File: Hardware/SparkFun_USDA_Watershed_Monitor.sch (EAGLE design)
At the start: 116 parts, among them J10 QWIIC_RIGHT_ANGLE, J3 QWIIC_RIGHT_ANGLE, J4 U.FL, J5 RJ45, J7 RJ45, J9 RJ45, Q1 20V/4.2A/52mΩ/1.4W, Q2 20V/0.2A/8MHz/1.2Ω/1Vth, Q3 20V/0.2A/8MHz/1.2Ω/1Vth, Q4 20V/0.2A/8MHz/1.2Ω/1Vth, Q5 20V/4.2A/52mΩ/1.4W, Q7 20V/4.2A/52mΩ/1.4W, U1 ESP-WROOM-3232D, U10 MMC5983MA_QFN16, U11 RFM9XRFM95, U12 NAU7802SOIC, U2 AP3429A, U3 MCP73831, U5 BME680, U6 9DoF IMU, U7 1.8V/100mA, U8 CH340C, U9 ISM330DHCX

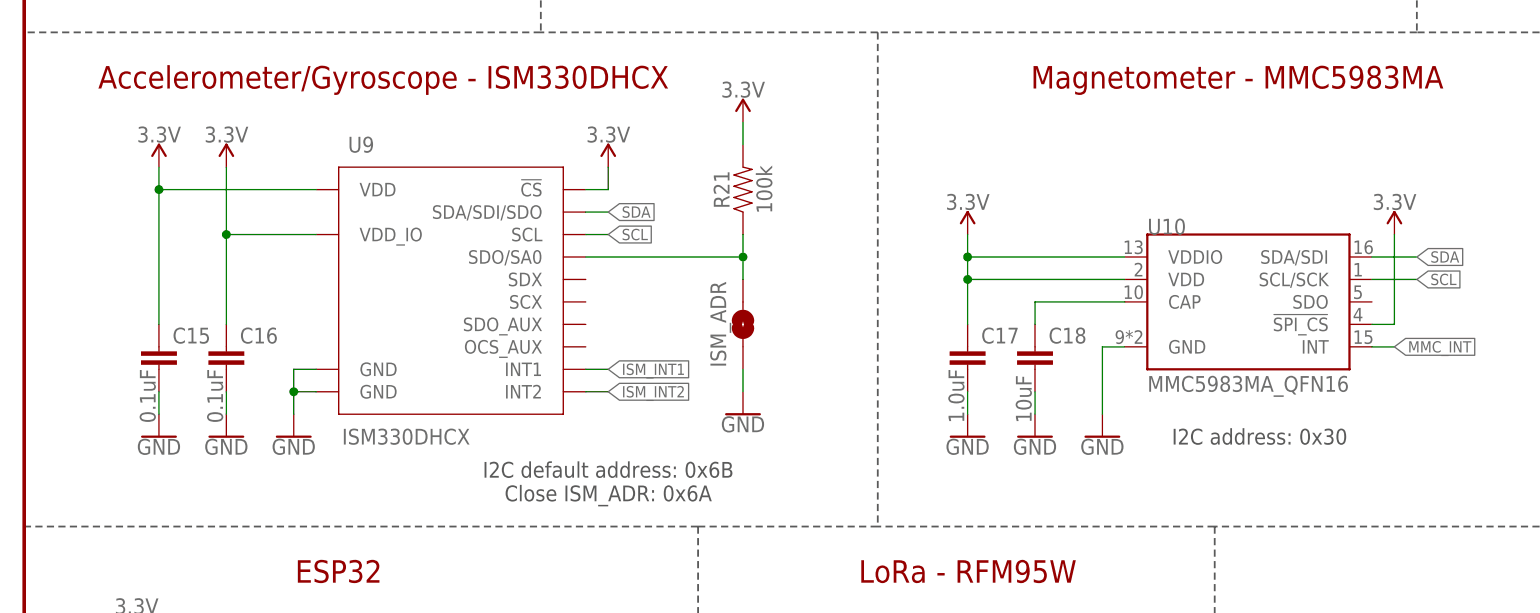
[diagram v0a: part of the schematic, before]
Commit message: Update DNP component values and PROD_ID's
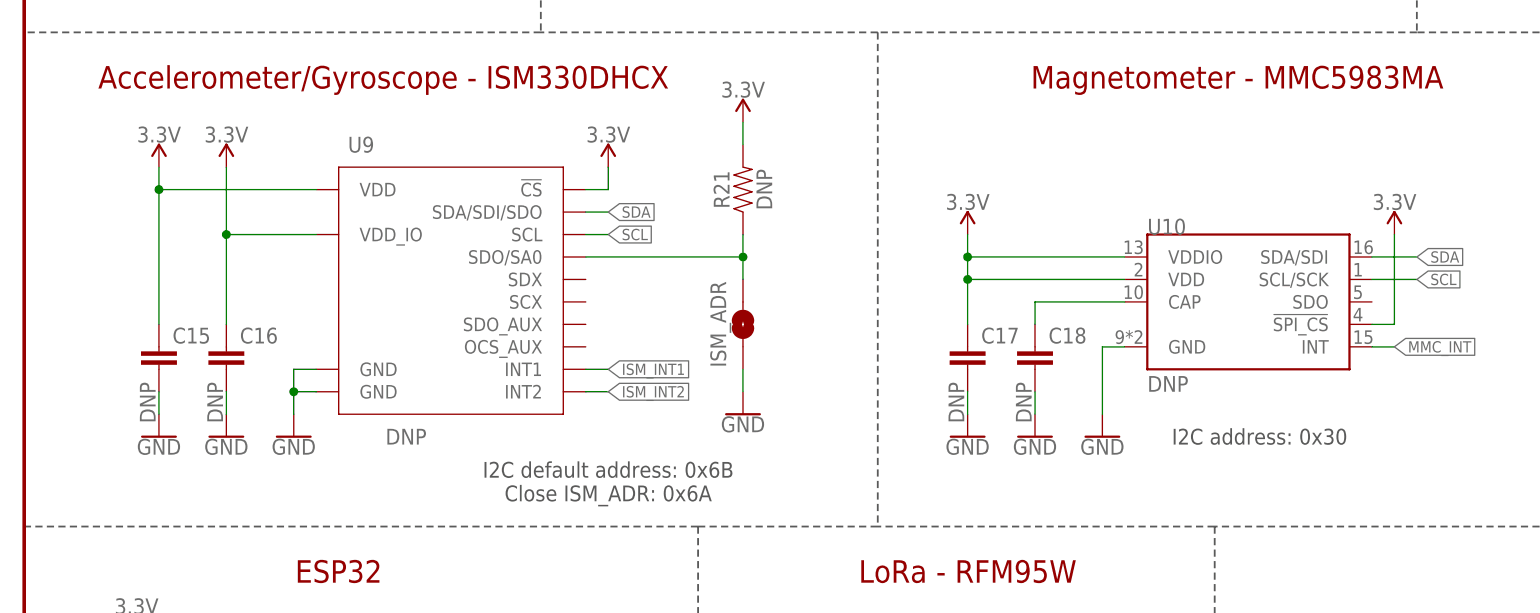
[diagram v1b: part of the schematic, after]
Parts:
- C15, C16: value 0.1uF -> DNP
- C17: value 1.0uF -> DNP
- C18: value 10uF -> DNP
- R21: value 100k -> DNP
- U10: value MMC5983MA_QFN16 -> DNP
- U9: value ISM330DHCX -> DNP
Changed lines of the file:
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@@
 <part name="SUPPLY31" library="SparkFun-PowerSymbols" deviceset="3.3V" device=""/>
 <part name="GND35" library="SparkFun-PowerSymbols" deviceset="GND" device=""/>
-<part name="U9" library="SparkFun-Sensors" deviceset="ISM330DHCX" device=""/>
-<part name="U10" library="SparkFun-Sensors" deviceset="MMC5983MA" device="_QFN16"/>
+<part name="U9" library="SparkFun-Sensors" deviceset="ISM330DHCX" device="" value="DNP">
+<attribute name="PROD_ID" value=""/>
+</part>
+<part name="U10" library="SparkFun-Sensors" deviceset="MMC5983MA" device="_QFN16" value="DNP">
+<attribute name="PROD_ID" value=""/>
+</part>
 <part name="SUPPLY34" library="SparkFun-PowerSymbols" deviceset="3.3V" device=""/>
 <part name="SUPPLY35" library="SparkFun-PowerSymbols" deviceset="3.3V" device=""/>
@@
 <part name="GND37" library="SparkFun-PowerSymbols" deviceset="GND" device=""/>
 <part name="GND38" library="SparkFun-PowerSymbols" deviceset="GND" device=""/>
-<part name="C15" library="SparkFun-Capacitors" deviceset="0.1UF" device="-0603-25V-(+80/-20%)" value="0.1uF"/>
-<part name="C16" library="SparkFun-Capacitors" deviceset="0.1UF" device="-0603-25V-(+80/-20%)" value="0.1uF"/>
+<part name="C15" library="SparkFun-Capacitors" deviceset="0.1UF" device="-0603-25V-(+80/-20%)" value="DNP">
+<attribute name="PROD_ID" value=""/>
+</part>
+<part name="C16" library="SparkFun-Capacitors" deviceset="0.1UF" device="-0603-25V-(+80/-20%)" value="DNP">
+<attribute name="PROD_ID" value=""/>
+</part>
 <part name="GND41" library="SparkFun-PowerSymbols" deviceset="GND" device=""/>
-<part name="C17" library="SparkFun-Capacitors" deviceset="1.0UF" device="-0603-16V-10%" value="1.0uF"/>
-<part name="C18" library="SparkFun-Capacitors" deviceset="10UF" device="-0603-6.3V-20%" value="10uF"/>
+<part name="C17" library="SparkFun-Capacitors" deviceset="1.0UF" device="-0603-16V-10%" value="DNP">
+<attribute name="PROD_ID" value=""/>
+</part>
+<part name="C18" library="SparkFun-Capacitors" deviceset="10UF" device="-0603-6.3V-20%" value="DNP">
+<attribute name="PROD_ID" value=""/>
+</part>
 <part name="GND39" library="SparkFun-PowerSymbols" deviceset="GND" device=""/>
 <part name="GND40" library="SparkFun-PowerSymbols" deviceset="GND" device=""/>
-<part name="R21" library="SparkFun-Resistors" deviceset="100KOHM" device="-0603-1/10W-1%" value="100k"/>
+<part name="R21" library="SparkFun-Resistors" deviceset="100KOHM" device="-0603-1/10W-1%" value="DNP">
+<attribute name="PROD_ID" value=""/>
+</part>
 <part name="SUPPLY37" library="SparkFun-PowerSymbols" deviceset="3.3V" device=""/>
 <part name="GND42" library="SparkFun-PowerSymbols" deviceset="GND" device=""/>

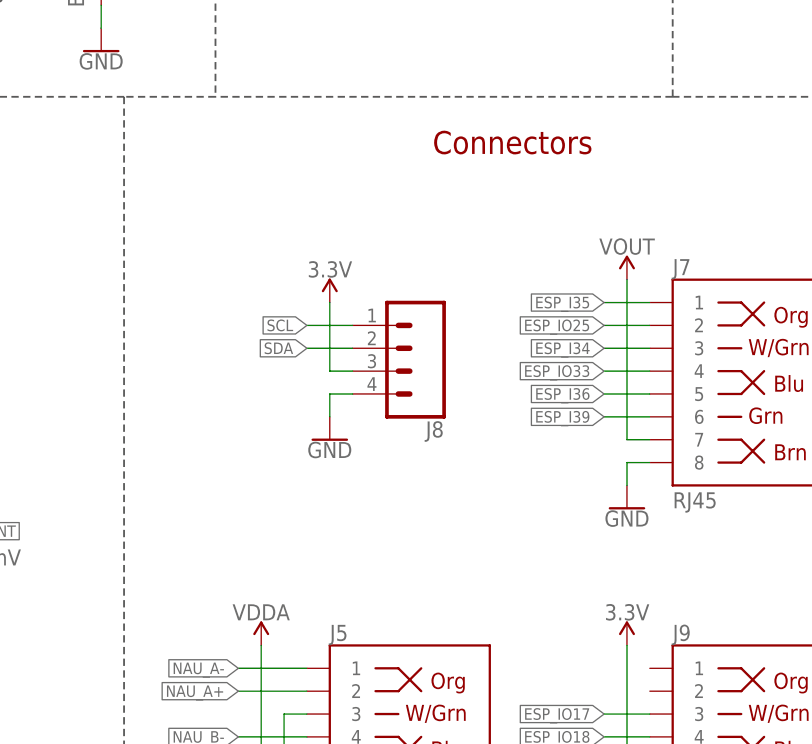
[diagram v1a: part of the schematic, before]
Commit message: Add 3-pin JST connector for GPS
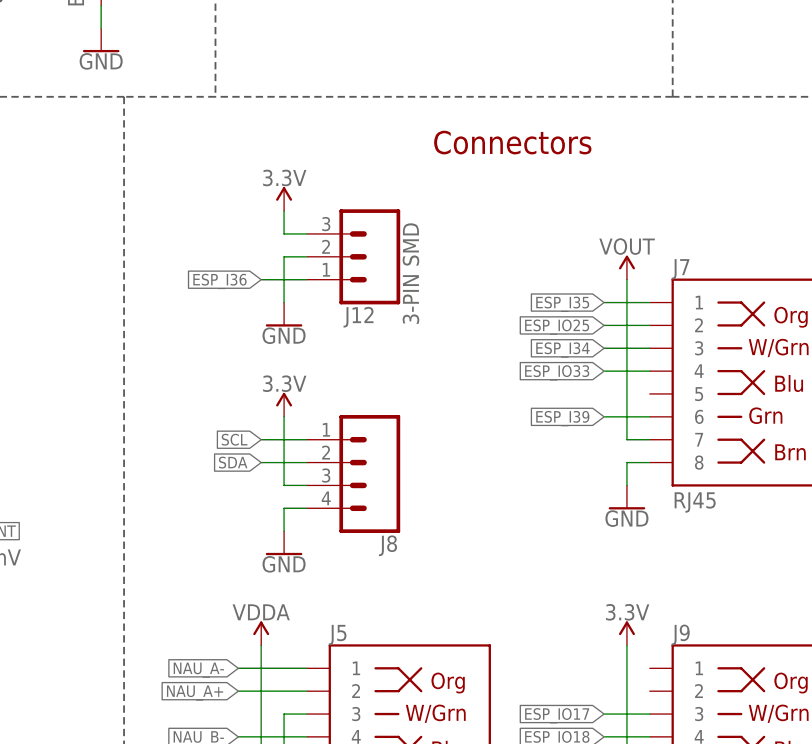
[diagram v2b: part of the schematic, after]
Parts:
- added J12: 3-PIN SMD, SparkFun-Connectors:CONN_03JST-SMD
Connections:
- net 3.3V: now also J12.1
- net ESP_I36: now also J12.3; no longer J7.5
- net GND: now also J12.2
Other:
- moved on the sheet: J8
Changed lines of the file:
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@@
 <part name="SUPPLY10" library="SparkFun-PowerSymbols" deviceset="VOUT" device=""/>
 <part name="R27" library="SparkFun-Resistors" deviceset="100KOHM" device="-0603-1/10W-1%" value="100k"/>
+<part name="J12" library="SparkFun-Connectors" deviceset="CONN_03" device="JST-SMD" value="3-PIN SMD"/>
+<part name="GND61" library="SparkFun-PowerSymbols" deviceset="GND" device=""/>
+<part name="SUPPLY41" library="SparkFun-PowerSymbols" deviceset="3.3V" device=""/>
 </parts>
 <sheets>
@@
 <attribute name="VALUE" x="281.94" y="198.374" size="1.778" layer="96" font="vector" align="bottom-center"/>
 </instance>
-<instance part="J8" gate="J1" x="276.86" y="66.04" smashed="yes" rot="R180">
-<attribute name="VALUE" x="281.94" y="73.406" size="1.778" layer="96" font="vector" rot="R180"/>
-<attribute name="NAME" x="281.94" y="57.912" size="1.778" layer="95" font="vector" rot="R180"/>
+<instance part="J8" gate="J1" x="271.78" y="53.34" smashed="yes" rot="R180">
+<attribute name="VALUE" x="276.86" y="60.706" size="1.778" layer="96" font="vector" rot="R180"/>
+<attribute name="NAME" x="276.86" y="45.212" size="1.778" layer="95" font="vector" rot="R180"/>
 </instance>
 <instance part="J11" gate="G$1" x="48.26" y="259.08" smashed="yes" rot="R180">
@@
 <attribute name="VALUE" x="320.04" y="233.426" size="1.778" layer="96" font="vector" align="top-center"/>
 </instance>
-<instance part="GND59" gate="1" x="269.24" y="55.88" smashed="yes" rot="MR0">
-<attribute name="VALUE" x="269.24" y="55.626" size="1.778" layer="96" font="vector" rot="MR0" align="top-center"/>
-</instance>
-<instance part="SUPPLY6" gate="G$1" x="269.24" y="71.12" smashed="yes" rot="MR0">
-<attribute name="VALUE" x="269.24" y="73.914" size="1.778" layer="96" font="vector" rot="MR0" align="bottom-center"/>
+<instance part="GND59" gate="1" x="264.16" y="43.18" smashed="yes" rot="MR0">
+<attribute name="VALUE" x="264.16" y="42.926" size="1.778" layer="96" font="vector" rot="MR0" align="top-center"/>
+</instance>
+<instance part="SUPPLY6" gate="G$1" x="264.16" y="58.42" smashed="yes" rot="MR0">
+<attribute name="VALUE" x="264.16" y="61.214" size="1.778" layer="96" font="vector" rot="MR0" align="bottom-center"/>
 </instance>
 <instance part="R26" gate="G$1" x="358.14" y="78.74" smashed="yes" rot="R90">
@@
 <attribute name="NAME" x="270.256" y="121.92" size="1.778" layer="95" font="vector" rot="R90" align="bottom-center"/>
 <attribute name="VALUE" x="273.304" y="121.92" size="1.778" layer="96" font="vector" rot="R90" align="top-center"/>
+</instance>
+<instance part="J12" gate="J$1" x="274.32" y="76.2" smashed="yes" rot="R180">
+<attribute name="VALUE" x="279.146" y="68.58" size="1.778" layer="96" font="vector" rot="R90"/>
+<attribute name="NAME" x="274.32" y="70.612" size="1.778" layer="95" font="vector" rot="R180"/>
+</instance>
+<instance part="GND61" gate="1" x="264.16" y="68.58" smashed="yes">
+<attribute name="VALUE" x="264.16" y="68.326" size="1.778" layer="96" font="vector" align="top-center"/>
+</instance>
+<instance part="SUPPLY41" gate="G$1" x="264.16" y="81.28" smashed="yes">
+<attribute name="VALUE" x="264.16" y="84.074" size="1.778" layer="96" font="vector" align="bottom-center"/>
 </instance>
 </instances>
@@
 <segment>
 <pinref part="GND59" gate="1" pin="GND"/>
-<wire x1="271.78" y1="60.96" x2="269.24" y2="60.96" width="0.1524" layer="91"/>
-<wire x1="269.24" y1="60.96" x2="269.24" y2="58.42" width="0.1524" layer="91"/>
+<wire x1="266.7" y1="48.26" x2="264.16" y2="48.26" width="0.1524" layer="91"/>
+<wire x1="264.16" y1="48.26" x2="264.16" y2="45.72" width="0.1524" layer="91"/>
 <pinref part="J8" gate="J1" pin="4"/>
 </segment>
@@
 <wire x1="231.14" y1="175.26" x2="231.14" y2="177.8" width="0.1524" layer="91"/>
 <pinref part="Q4" gate="NMOS" pin="S"/>
+</segment>
+<segment>
+<pinref part="GND61" gate="1" pin="GND"/>
+<pinref part="J12" gate="J$1" pin="2"/>
+<wire x1="264.16" y1="71.12" x2="264.16" y2="76.2" width="0.1524" layer="91"/>
+<wire x1="264.16" y1="76.2" x2="266.7" y2="76.2" width="0.1524" layer="91"/>
 </segment>
 </net>
@@
 <segment>
 <pinref part="SUPPLY6" gate="G$1" pin="3.3V"/>
-<wire x1="271.78" y1="63.5" x2="269.24" y2="63.5" width="0.1524" layer="91"/>
-<wire x1="269.24" y1="63.5" x2="269.24" y2="71.12" width="0.1524" layer="91"/>
+<wire x1="266.7" y1="50.8" x2="264.16" y2="50.8" width="0.1524" layer="91"/>
+<wire x1="264.16" y1="50.8" x2="264.16" y2="58.42" width="0.1524" layer="91"/>
 <pinref part="J8" gate="J1" pin="3"/>
 </segment>
@@
 <junction x="271.78" y="129.54"/>
 </segment>
+<segment>
+<pinref part="J12" gate="J$1" pin="1"/>
+<pinref part="SUPPLY41" gate="G$1" pin="3.3V"/>
+<wire x1="266.7" y1="78.74" x2="264.16" y2="78.74" width="0.1524" layer="91"/>
+<wire x1="264.16" y1="78.74" x2="264.16" y2="81.28" width="0.1524" layer="91"/>
+</segment>
 </net>
 <net name="N$8" class="0">
@@
 </segment>
 <segment>
-<wire x1="271.78" y1="68.58" x2="266.7" y2="68.58" width="0.1524" layer="91"/>
-<label x="266.7" y="68.58" size="1.27" layer="95" font="vector" rot="MR0" xref="yes"/>
+<wire x1="266.7" y1="55.88" x2="261.62" y2="55.88" width="0.1524" layer="91"/>
+<label x="261.62" y="55.88" size="1.27" layer="95" font="vector" rot="MR0" xref="yes"/>
 <pinref part="J8" gate="J1" pin="1"/>
 </segment>
@@
 </segment>
 <segment>
-<label x="266.7" y="66.04" size="1.27" layer="95" font="vector" rot="MR0" xref="yes"/>
-<wire x1="271.78" y1="66.04" x2="266.7" y2="66.04" width="0.1524" layer="91"/>
+<label x="261.62" y="53.34" size="1.27" layer="95" font="vector" rot="MR0" xref="yes"/>
+<wire x1="266.7" y1="53.34" x2="261.62" y2="53.34" width="0.1524" layer="91"/>
 <pinref part="J8" gate="J1" pin="2"/>
 </segment>
@@
 </segment>
 <segment>
-<wire x1="304.8" y1="60.96" x2="299.72" y2="60.96" width="0.1524" layer="91"/>
-<label x="299.72" y="60.96" size="1.27" layer="95" font="vector" rot="R180" xref="yes"/>
-<pinref part="J7" gate="JP1" pin="5"/>
-</segment>
-</net>
+<wire x1="266.7" y1="73.66" x2="261.62" y2="73.66" width="0.1524" layer="91"/>
+<label x="261.62" y="73.66" size="1.27" layer="95" font="vector" rot="R180" xref="yes"/>
+<pinref part="J12" gate="J$1" pin="3"/>
+</segment>
+</net>

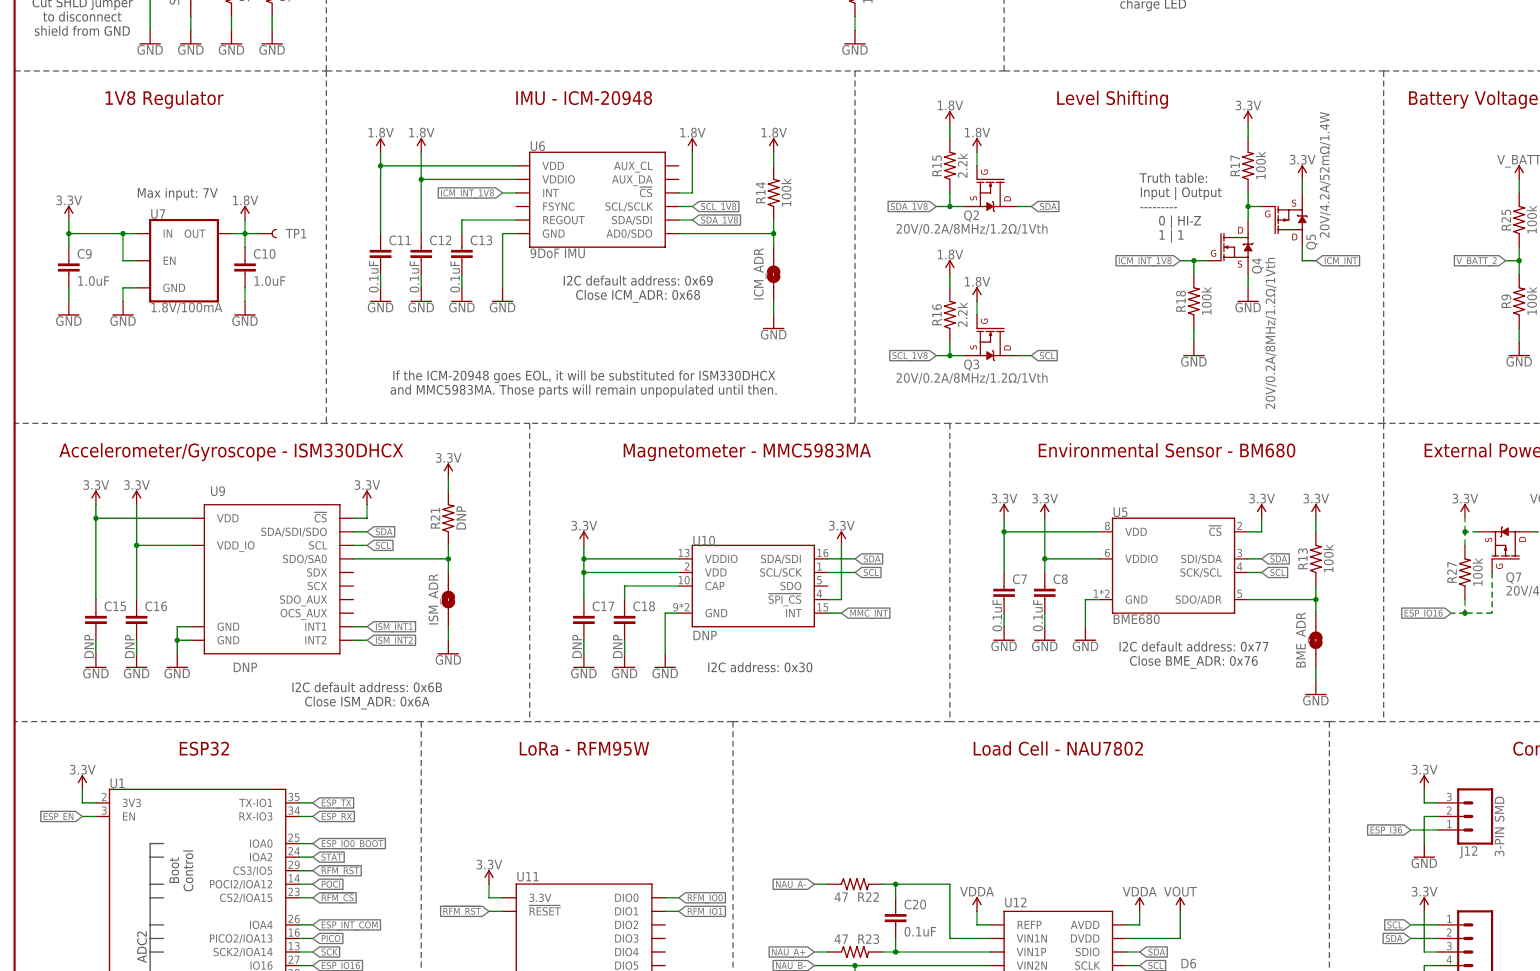
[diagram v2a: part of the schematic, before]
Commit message: Connect all onboard sensors and LoRa to VOUT
Helps achieve lower power
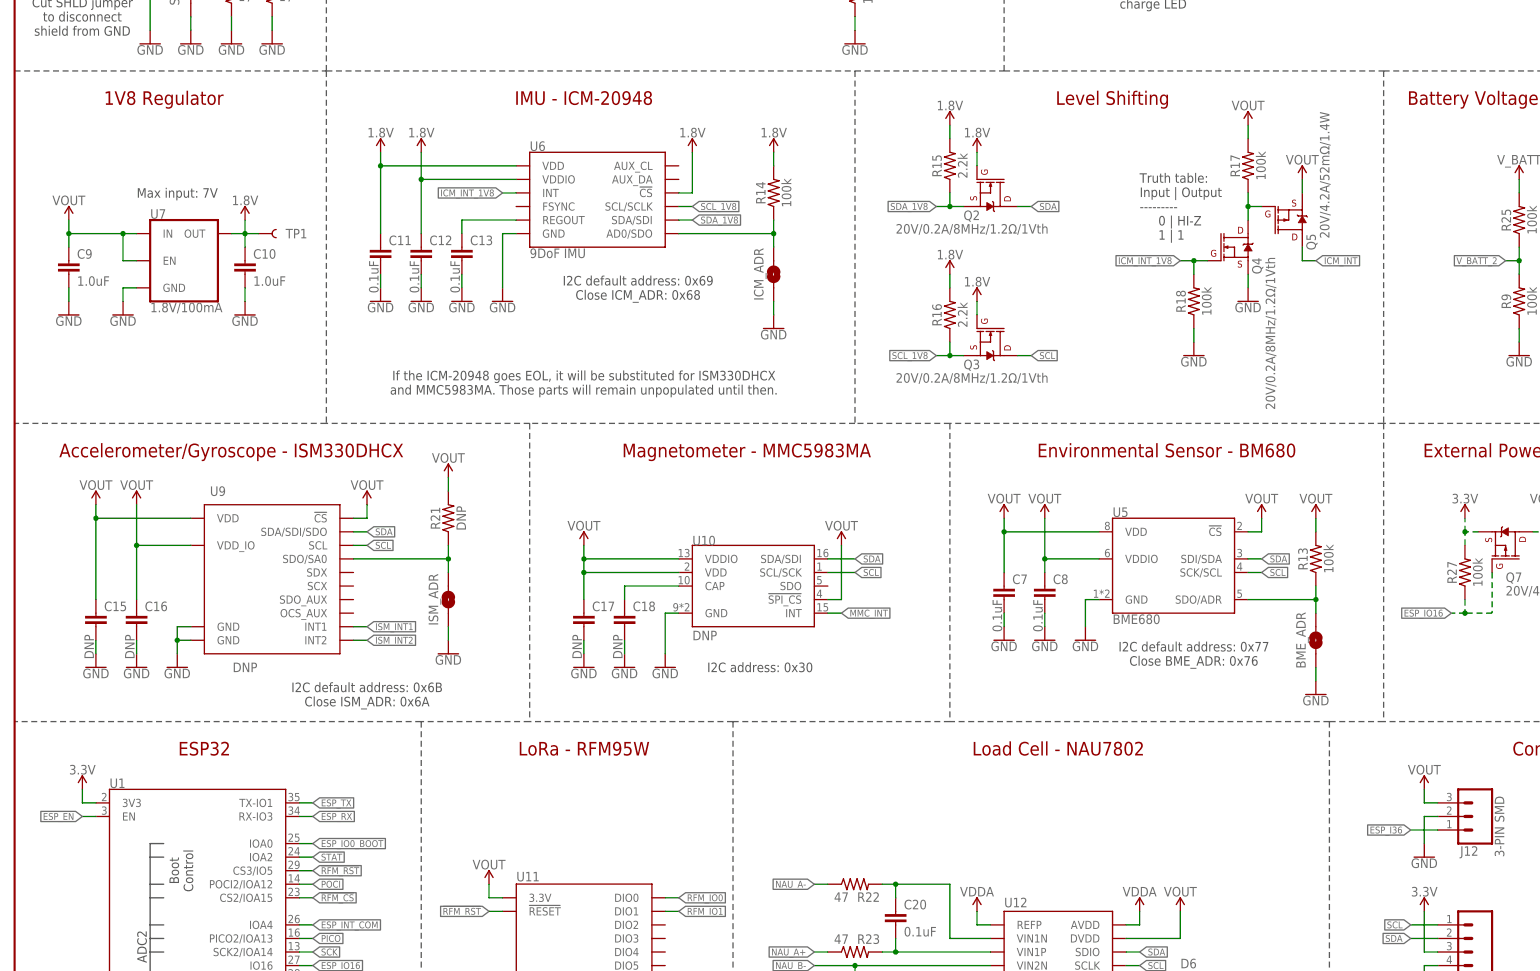
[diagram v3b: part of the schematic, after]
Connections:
- net 3.3V: no longer C15.1, C16.1, C17.1, C7.1, C8.1, C9.1, J12.1, Q5.S, R13.2, R17.2, R21.2, U10.!SPI_CS!, U10.VDD, U10.VDDIO, U11.3.3V, U5.!CS, U5.VDD, U5.VDDIO, U7.EN, U7.IN, U9.!CS!, U9.VDD, U9.VDD_IO
- net VOUT: now also C15.1, C16.1, C17.1, C7.1, C8.1, C9.1, J12.1, Q5.S, R13.2, R17.2, R21.2, U10.!SPI_CS!, U10.VDD, U10.VDDIO, U11.3.3V, U5.!CS, U5.VDD, U5.VDDIO, U7.EN, U7.IN, U9.!CS!, U9.VDD, U9.VDD_IO
